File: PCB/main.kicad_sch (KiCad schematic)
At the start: 62 parts, among them J1 S20B-PADSS-1, J2 S20B-PADSS-1, J3 SWD, SW1 SPST, U2 AMS1117-3.3, U3 MCP2558FD, U4 MCP2558FD, U5 STM32G0B1, U6 TPS54302, Y1 ${Frequency}

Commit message: Start changing LDO
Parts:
- added C1: ${Capacitance}, Capacitor_SMD:C_0805_2012Metric, symbol 0 Passive_Components:Capacitors/CMP-0020
- added C2: ${Capacitance}, Capacitor_SMD:C_1206_3216Metric, symbol 0 Passive_Components:Capacitors/CMP-0031
- added D1: LED_B, LED_SMD:LED_0603_1608Metric, symbol 0 Opto_Electronics:LEDs/CMP-0023
- added R1: ${Resistance}, Resistor_SMD:R_0402_1005Metric, symbol 0 Passive_Components:Resistors/CMP-0024
- added U1: XC6206P33, libdb:CMP-0019, symbol 0 Power_Management:LDO Regulators/CMP-0019
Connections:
- net +3.3V: now also C2.1, R1.2, U1.2 (VO)
- net GND: now also C1.2, C2.2, D1.1 (K), U1.1 (GND)
- new net: C1.1, U1.3 (VI)
- new net: D1.2 (A), R1.1
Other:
- moved on the sheet: C20, C22, C23, C24, C25, C26, C7, C8, C9, D3, D5, L2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

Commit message: Further development, started final GND pour
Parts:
- removed C7, C8, C9: ${Capacitance}, Capacitor_Tantalum_SMD:CP_EIA-3216-18_Kemet-A, symbol 0 Passive_Components:Capacitors/CMP-0029
- removed D3: LED_B, LED_SMD:LED_0603_1608Metric, symbol 0 Opto_Electronics:LEDs/CMP-0023
- removed R4: ${Resistance}, Resistor_SMD:R_0402_1005Metric, symbol 0 Passive_Components:Resistors/CMP-0024
- removed U2: AMS1117-3.3, Package_TO_SOT_SMD:SOT-223-3_TabPin2, symbol 0 Power_Management:LDO Regulators/CMP-0027
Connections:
- net +3.3V: now also D1.2 (A); no longer R1.2
- net +5V: now also C1.1, U1.3 (VI)
- net GND: now also R1.1; no longer D1.1 (K)
- new net: D1.1 (K), R1.2
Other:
- moved on the sheet: C1, C2, C20, C22, C23, C24, C25, C26, D1, D5, L2, R1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

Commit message: Generate gerbers
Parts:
- removed ART1: Cat (small, mirrored), libdb:CMP-0044, symbol 0 Other:Artwork/CMP-0044
- removed ART2: Dog (small), libdb:CMP-0045, symbol 0 Other:Artwork/CMP-0045
- removed ART3: JLCJLCJLCJLC, libdb:CMP-0047, symbol 0 Other:Artwork/CMP-0047
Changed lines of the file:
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@@
-    )
-  )
-  (symbol (lib_id "0 Other:Artwork/CMP-0045") (at 217.17 25.4 0) (unit 1)
-    (in_bom no) (on_board yes) (dnp no) (fields_autoplaced)
-    (property "Reference" "ART2" (at 224.79 24.635 0)
-      (effects (font (size 1.27 1.27)) (justify left))
-    )
-    (property "Value" "Dog (small)" (at 224.79 27.175 0)
-      (effects (font (size 1.27 1.27)) (justify left))
-    )
-    (property "Footprint" "libdb:CMP-0045" (at 217.17 16.51 0)
-      (effects (font (size 1.27 1.27)) hide)
-    )
-    (property "Datasheet" "" (at 217.17 16.51 0)
-      (effects (font (size 1.27 1.27)) hide)
-    )
-    (instances
-      (project "main"
-        (path "/4f4cf64f-c95a-4a4a-b388-e87470ab2a3e"
-          (reference "ART2") (unit 1)
-        )
-      )
     )
   )
@@
     )
   )
-  (symbol (lib_id "0 Other:Artwork/CMP-0047") (at 246.38 25.4 0) (unit 1)
-    (in_bom no) (on_board yes) (dnp no) (fields_autoplaced)
-    (property "Reference" "ART3" (at 254 24.635 0)
-      (effects (font (size 1.27 1.27)) (justify left))
-    )
-    (property "Value" "JLCJLCJLCJLC" (at 254 27.175 0)
-      (effects (font (size 1.27 1.27)) (justify left))
-    )
-    (property "Footprint" "libdb:CMP-0047" (at 246.38 16.51 0)
-      (effects (font (size 1.27 1.27)) hide)
-    )
-    (property "Datasheet" "" (at 246.38 16.51 0)
-      (effects (font (size 1.27 1.27)) hide)
-    )
-    (instances
-      (project "main"
-        (path "/4f4cf64f-c95a-4a4a-b388-e87470ab2a3e"
-          (reference "ART3") (unit 1)
-        )
-      )
-    )
-  )
   (symbol (lib_id "0 Electromechanical:Tactile Switches/CMP-0011") (at 187.96 77.47 270) (mirror x) (unit 1)
     (in_bom yes) (on_board yes) (dnp no)
@@
         )
       )
-    )
-  )
-  (symbol (lib_id "0 Other:Artwork/CMP-0044") (at 180.34 25.4 0) (unit 1)
-    (in_bom no) (on_board yes) (dnp no) (fields_autoplaced)
-    (property "Reference" "ART1" (at 187.96 24.635 0)
-      (effects (font (size 1.27 1.27)) (justify left))
-    )
-    (property "Value" "Cat (small, mirrored)" (at 187.96 27.175 0)
-      (effects (font (size 1.27 1.27)) (justify left))
-    )
-    (property "Footprint" "libdb:CMP-0044" (at 180.34 16.51 0)
-      (effects (font (size 1.27 1.27)) hide)
-    )
-    (property "Datasheet" "" (at 180.34 16.51 0)
-      (effects (font (size 1.27 1.27)) hide)
-    )
-    (instances
-      (project "main"
-        (path "/4f4cf64f-c95a-4a4a-b388-e87470ab2a3e"
-          (reference "ART1") (unit 1)
-        )
-      )

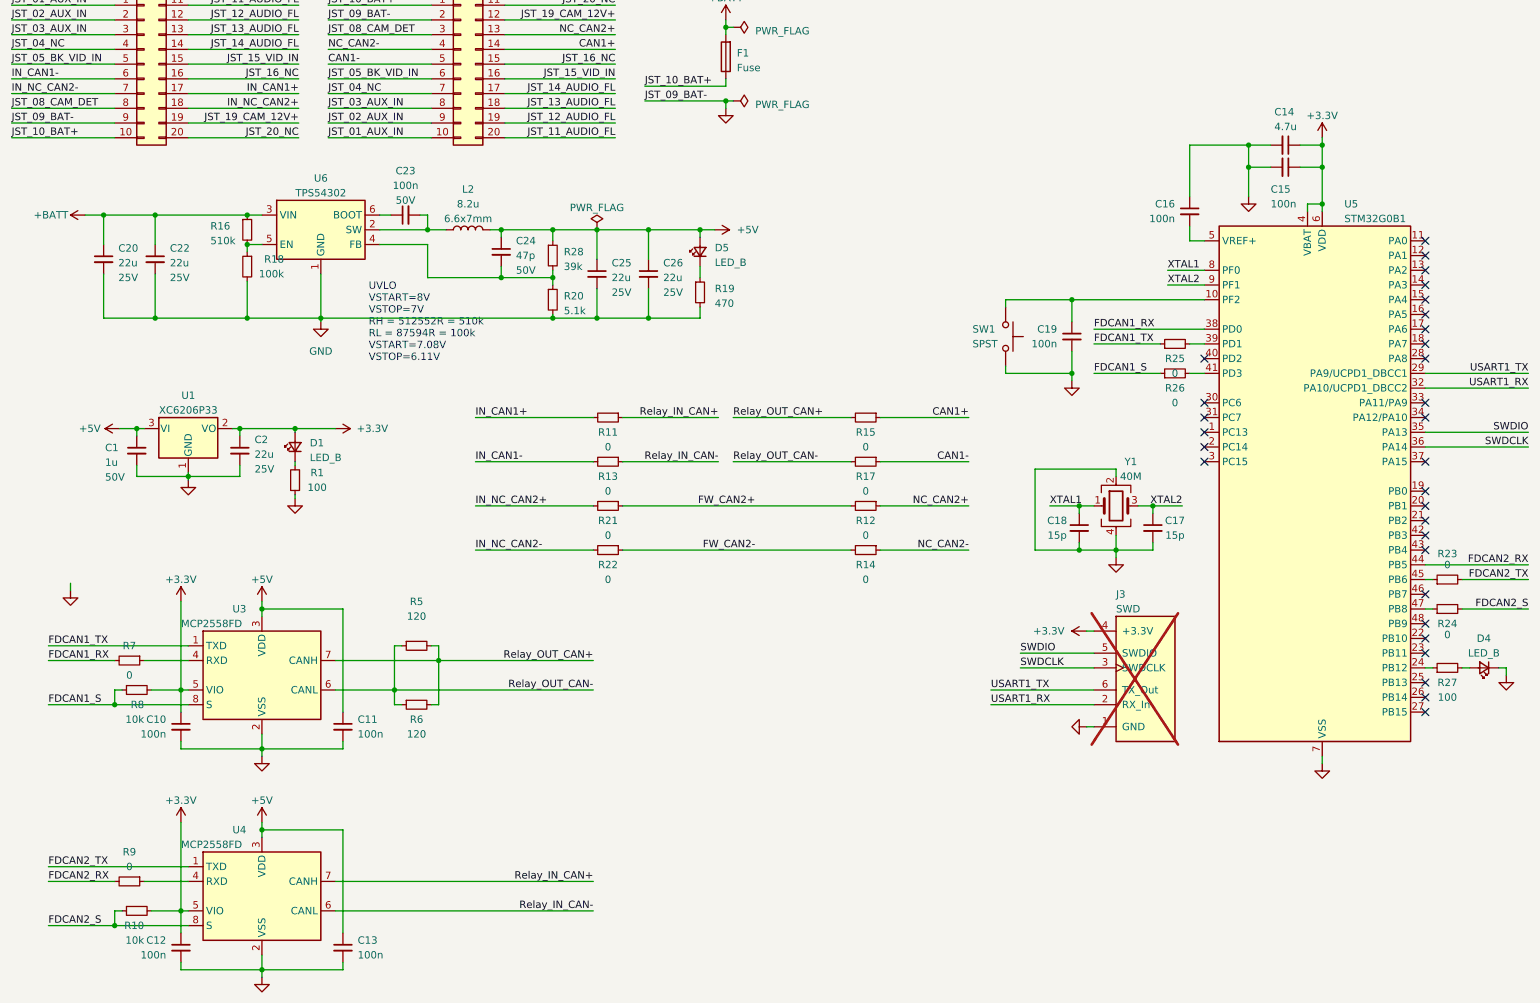
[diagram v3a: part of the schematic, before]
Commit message: Switch to TJA1051T/3
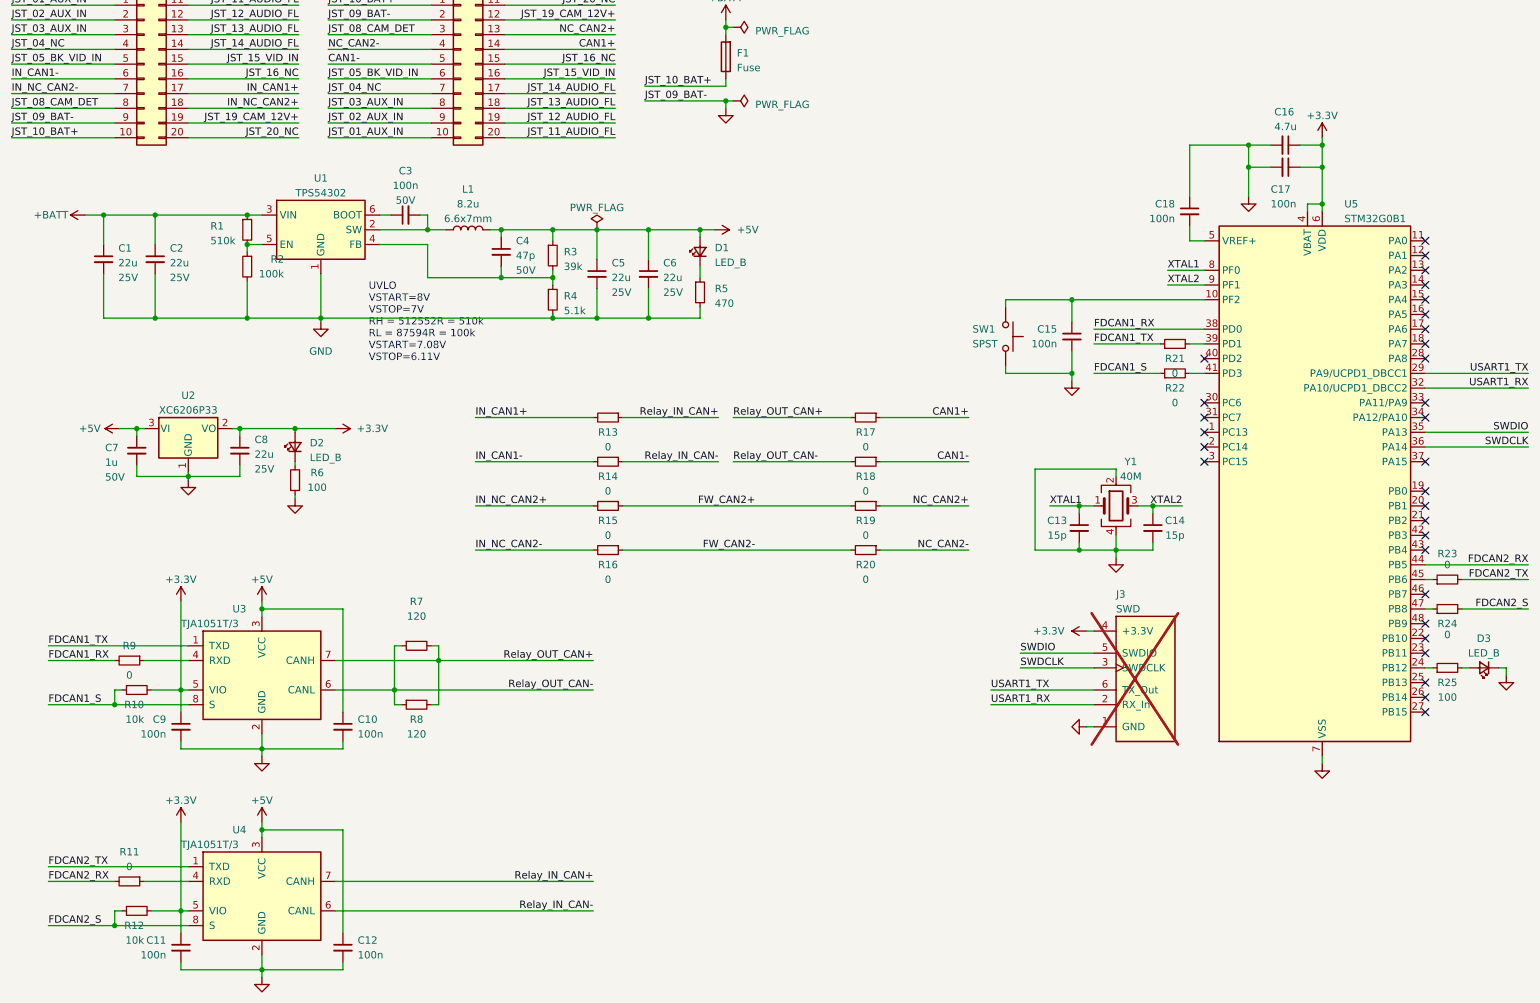
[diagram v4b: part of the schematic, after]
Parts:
- J3: now left out of the parts list
- U3, U4: value MCP2558FD -> TJA1051T/3; symbol 0 Interfaces:CAN Tranceivers/CMP-0002 -> 0 Interfaces:CAN Tranceivers/CMP-0069; LCSC C124015 -> C38695; MPN MCP2558FD-H/SN -> TJA1051T/3/1J; Manufacturer Microchip Technology -> NXP Semiconductors
- renumbered C20 to C1, C11 to C10, C12 to C11, C13 to C12, C18 to C13, C17 to C14, C19 to C15, C14 to C16, C15 to C17, C16 to C18, C22 to C2, C23 to C3, C24 to C4, C25 to C5, C26 to C6, C1 to C7, C2 to C8, C10 to C9, D5 to D1, D1 to D2, D4 to D3, L2 to L1, R16 to R1, R8 to R10, R9 to R11, R10 to R12, R11 to R13, R13 to R14, R21 to R15, R22 to R16, R15 to R17, R17 to R18, R12 to R19, R18 to R2, R14 to R20, R25 to R21, R26 to R22, R27 to R25, R28 to R3, R20 to R4, R19 to R5, R1 to R6, R5 to R7, R6 to R8, R7 to R9, U6 to U1, U1 to U2

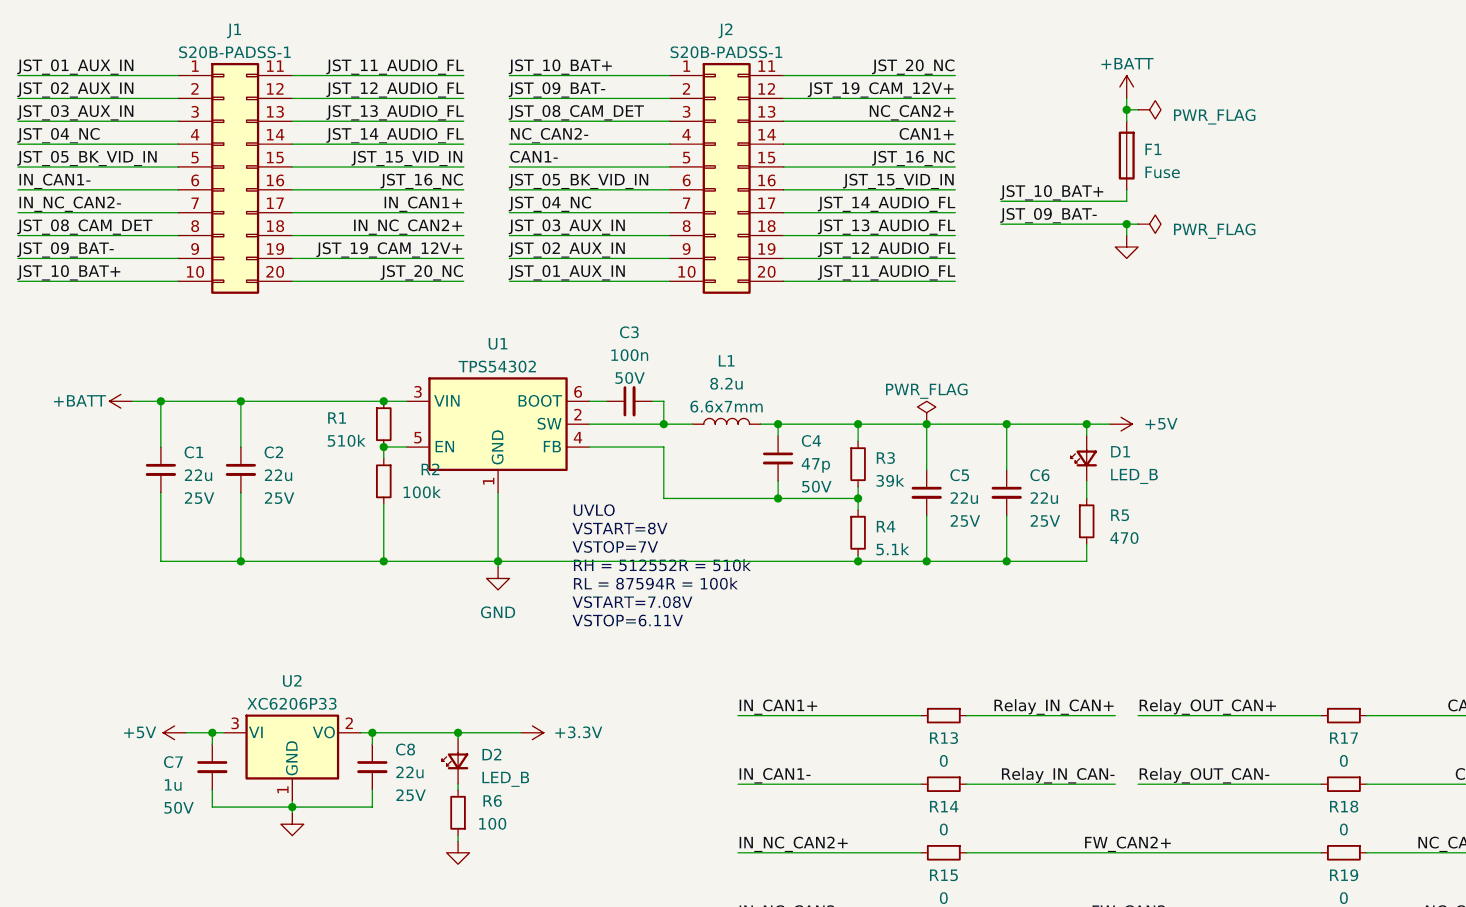
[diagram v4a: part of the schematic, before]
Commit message: Added bulk capacitance
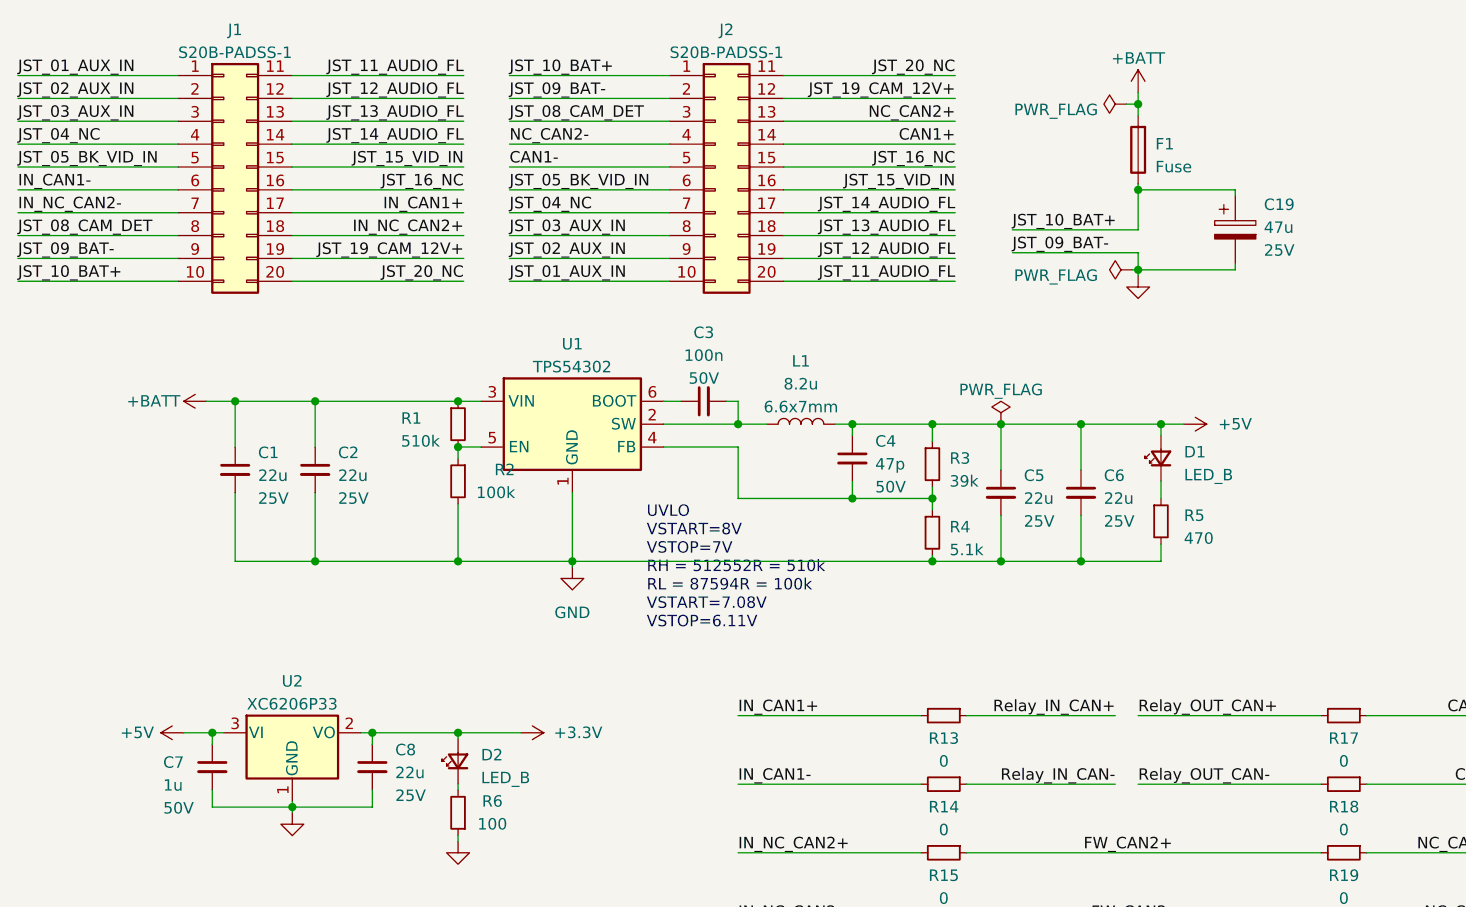
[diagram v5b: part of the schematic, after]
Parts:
- added C19: ${Capacitance}, Capacitor_SMD:CP_Elec_6.3x5.8, symbol 0 Passive_Components:Capacitors/CMP-0070
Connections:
- net GND: now also C19.2
- net JST_10_BAT+: now also C19.1
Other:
- moved on the sheet: C1, C2, C3, C4, C5, C6, D1, F1, L1, R1, R2, R3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
